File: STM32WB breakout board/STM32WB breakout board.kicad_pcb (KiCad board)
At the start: 2 copper layers, 70 x 80 mm, 37 parts, among them J1 Conn_02x10_Counter_Clockwise, J2 Conn_02x10_Counter_Clockwise, J3 RSP-122811-02, J4 Conn_02x10_Counter_Clockwise, J5 Conn_02x10_Counter_Clockwise, U1 STM32WB15CCU6, X1 32 MHz, X2 32.768 kHz

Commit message: PCB button updated
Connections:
- L2 pad 1: Net-(L2-Pad1) -> /RF & Power/VLXSMPS
- L2 pad 2: /RF & Power/VLXSMPS -> Net-(L2-Pad2)
- L3 pad 1: /RF & Power/VFBSMPS -> Net-(L2-Pad2)
- L3 pad 2: Net-(L2-Pad1) -> /RF & Power/VFBSMPS
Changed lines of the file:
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@@
   (net 36 "/RF & Power/VLXSMPS")
   (net 37 "unconnected-(U1-PB0-Pad28)")
-  (net 38 "Net-(L2-Pad1)")
+  (net 38 "Net-(L2-Pad2)")
   (net 39 "unconnected-(S1-NO_1-Pad1)")
   (net 40 "unconnected-(S1-COM_1-Pad3)")
@@
         (effects (font (size 1 1) (thickness 0.15)))
     )
-    (fp_text user "*" (at -4.491 -3.000756 unlocked) (layer "F.SilkS")
+    (fp_text user "*" (at -4.491 -3.000756) (layer "F.SilkS")
         (effects (font (size 1 1) (thickness 0.15)))
     )
-    (fp_text user "*" (at -4.491 -3.000756) (layer "F.SilkS")
+    (fp_text user "*" (at -4.491 -3.000756 unlocked) (layer "F.SilkS")
         (effects (font (size 1 1) (thickness 0.15)))
     )
@@
       (stroke (width 0.2) (type solid)) (fill none) (layer "F.Fab"))
     (pad "1" smd rect (at -0.468 0 180) (size 0.46 0.7) (layers "F.Cu" "F.Paste" "F.Mask")
-      (net 38 "Net-(L2-Pad1)") (pintype "passive") (solder_mask_margin 0.102))
-    (pad "2" smd rect (at 0.468 0 180) (size 0.46 0.7) (layers "F.Cu" "F.Paste" "F.Mask")
       (net 36 "/RF & Power/VLXSMPS") (pintype "passive") (solder_mask_margin 0.102))
+    (pad "2" smd rect (at 0.468 0 180) (size 0.46 0.7) (layers "F.Cu" "F.Paste" "F.Mask")
+      (net 38 "Net-(L2-Pad2)") (pintype "passive") (solder_mask_margin 0.102))
   )
   (footprint "Button_Switch_THT:TS026670BK160LCRD" (layer "F.Cu")
@@
     (property "ki_description" "Tactile Switches 6 x 6 mm, 7 mm Act Height, 160 gf, Black, Long Crimped, Through Hole, SPST,")
     (attr through_hole)
-    (fp_text reference "S1" (at 3.25 2.25) (layer "F.SilkS")
+    (fp_text reference "S1" (at 3.25 2.25 180) (layer "F.SilkS")
         (effects (font (size 1.27 1.27) (thickness 0.254)))
     )
-    (fp_text value "USER BUTTON" (at 3.25 2.25) (layer "F.SilkS") hide
+    (fp_text value "USER BUTTON" (at 3.25 2.25 180) (layer "F.SilkS") hide
         (effects (font (size 1.27 1.27) (thickness 0.254)))
     )
-    (fp_text user "${REFERENCE}" (at 3.25 2.25) (layer "F.Fab")
+    (fp_text user "${REFERENCE}" (at 3.25 2.25 180) (layer "F.Fab")
         (effects (font (size 1.27 1.27) (thickness 0.254)))
     )
@@
       (stroke (width 0.127) (type solid)) (layer "F.Fab"))
     (pad "1" smd rect (at -0.86 0 90) (size 1.2 1.47) (layers "F.Cu" "F.Paste" "F.Mask")
-      (net 35 "/RF & Power/VFBSMPS") (pintype "passive") (solder_mask_margin 0.102))
+      (net 38 "Net-(L2-Pad2)") (pintype "passive") (solder_mask_margin 0.102))
     (pad "2" smd rect (at 0.86 0 90) (size 1.2 1.47) (layers "F.Cu" "F.Paste" "F.Mask")
-      (net 38 "Net-(L2-Pad1)") (pintype "passive") (solder_mask_margin 0.102))
+      (net 35 "/RF & Power/VFBSMPS") (pintype "passive") (solder_mask_margin 0.102))
   )
   (footprint "GRM1555C1HR80BA01D:CAPC1005X55N" (layer "F.Cu")

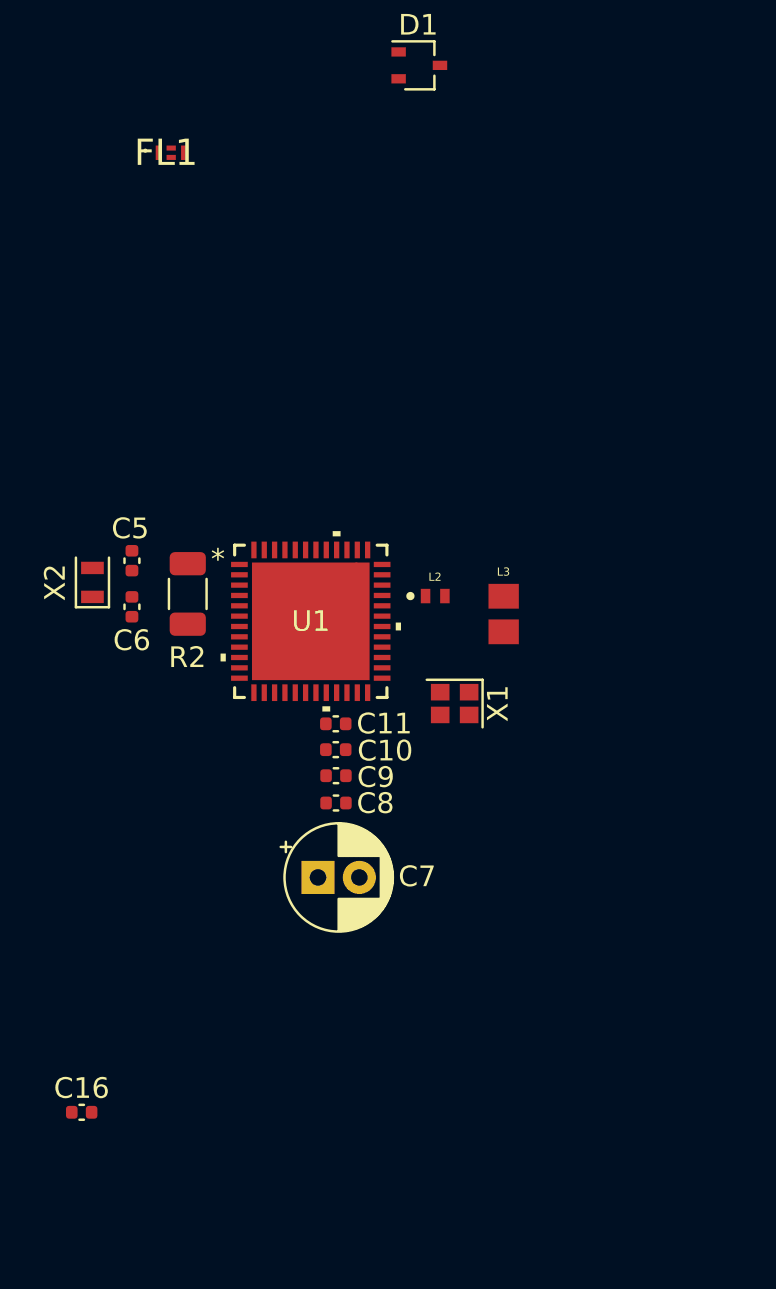
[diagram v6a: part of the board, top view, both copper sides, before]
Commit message: Regulator section updating
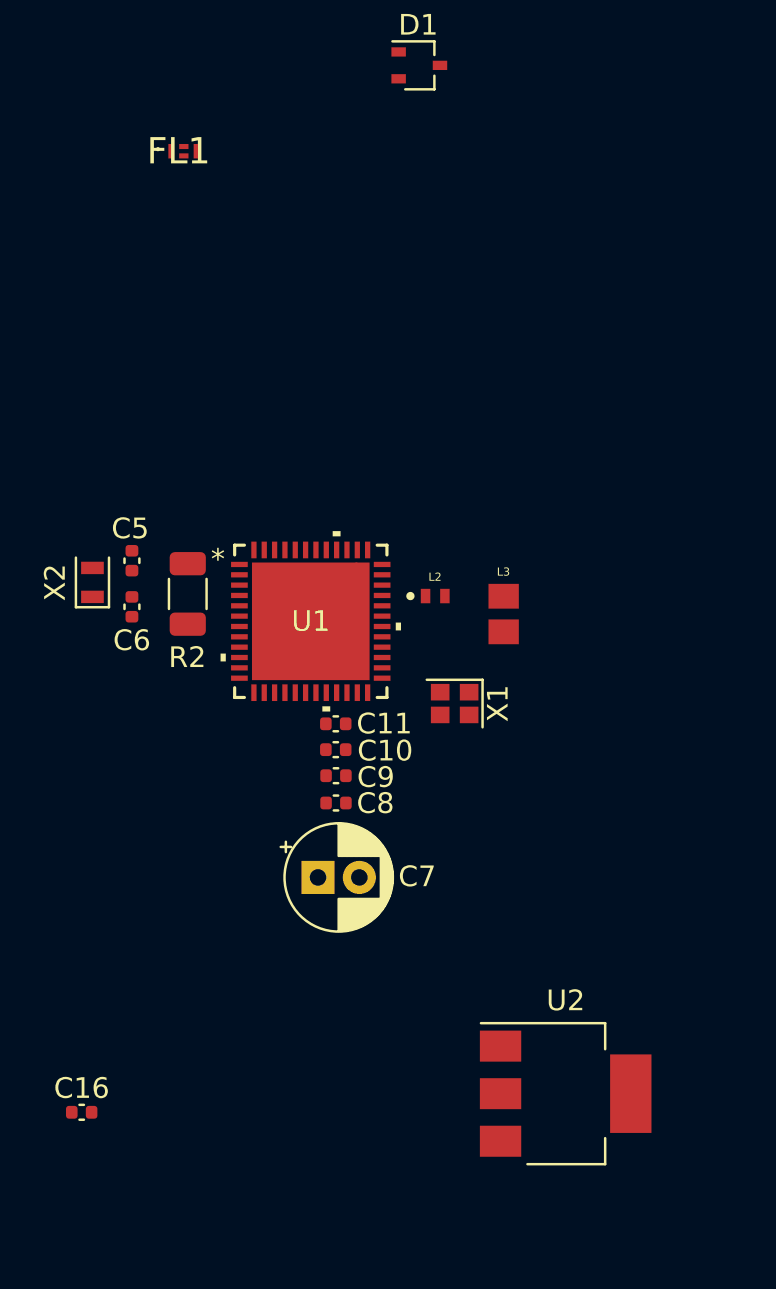
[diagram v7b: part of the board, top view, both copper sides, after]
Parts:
- added U2: AMS1117, Package_TO_SOT_SMD:SOT-223-3_TabPin2, F.Cu at (161.1, 117.7)
- moved FL1 0.61 mm to (142.6, 72.2)
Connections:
- net /RF & Power/RF1 renamed /RF & SMPS/RF1
- net /RF & Power/VFBSMPS renamed /RF & SMPS/VFBSMPS
- net /RF & Power/VLXSMPS renamed /RF & SMPS/VLXSMPS

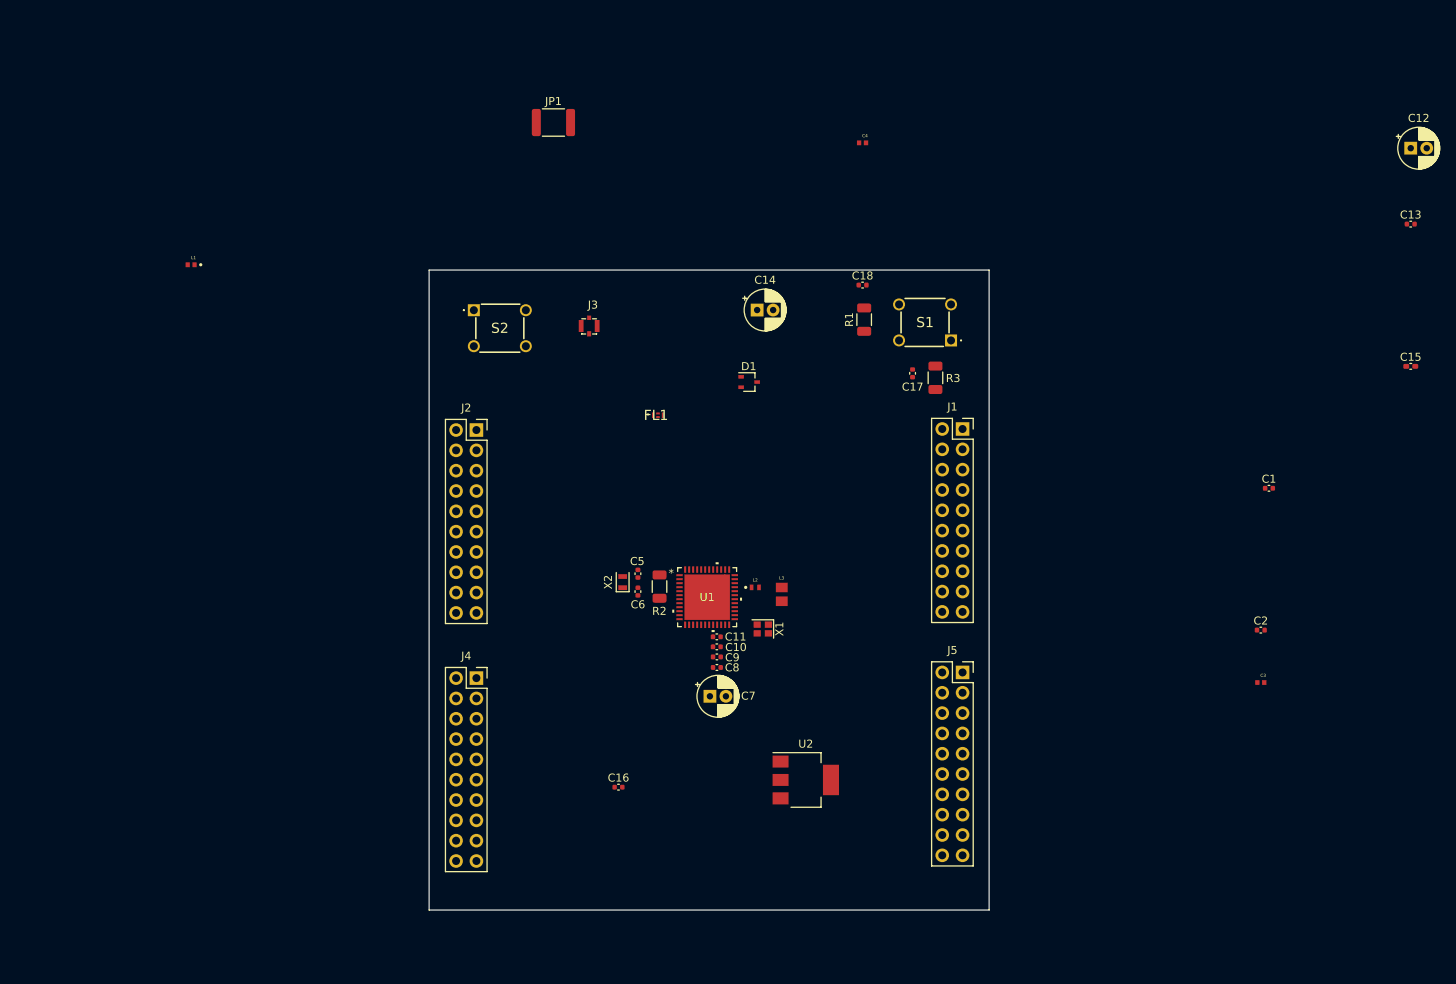
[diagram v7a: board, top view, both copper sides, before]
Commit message: Regulator section updating
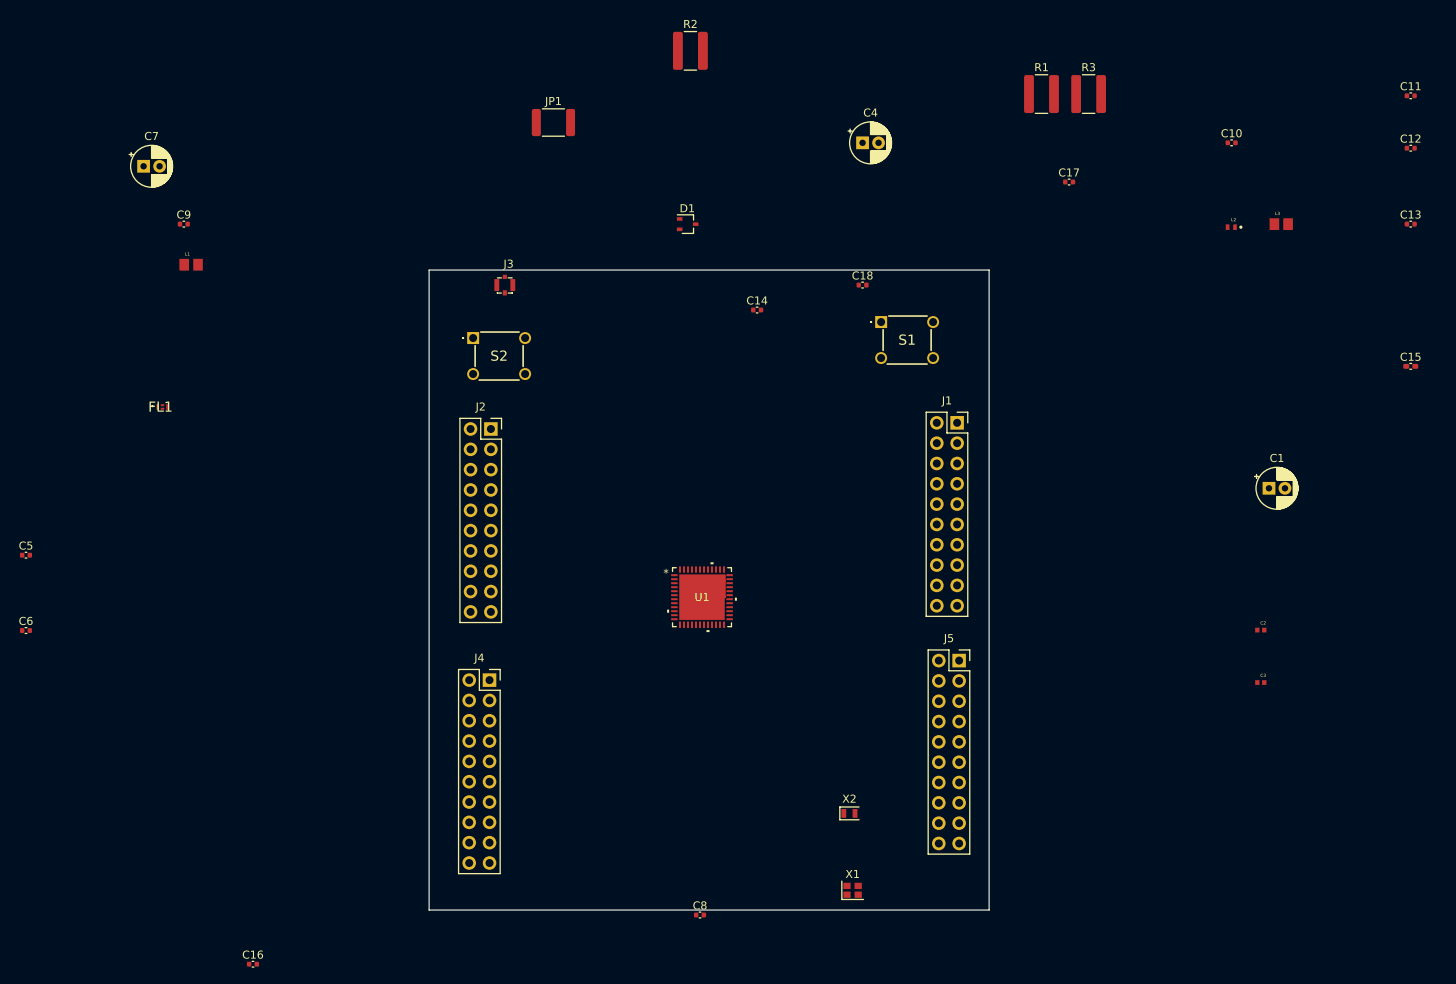
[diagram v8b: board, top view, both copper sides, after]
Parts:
- removed U2: AMS1117, Package_TO_SOT_SMD:SOT-223-3_TabPin2
- C1: value 100nF -> 4.7 uF; footprint Capacitor_SMD:C_0402_1005Metric -> Capacitor_THT:CP_Radial_D5.0mm_P2.00mm
- C12: value 4.7 uF -> 100nF; footprint Capacitor_THT:CP_Radial_D5.0mm_P2.00mm -> Capacitor_SMD:C_0402_1005Metric
- C14: value 4.7 uF -> 100 pF; footprint Capacitor_THT:CP_Radial_D5.0mm_P2.00mm -> Capacitor_SMD:C_0402_1005Metric
- C2: value 100 pF -> GRM1555C1HR80BA01D; footprint Capacitor_SMD:C_0402_1005Metric -> GRM1555C1HR80BA01D:CAPC1005X55N
- C3: value GRM1555C1HR80BA01D -> GRM1555C1HR30WA01D; footprint GRM1555C1HR80BA01D:CAPC1005X55N -> GRM1555C1HR30WA01D:CAPC1005X55N
- C4: value GRM1555C1HR30WA01D -> 4.7 uF; footprint GRM1555C1HR30WA01D:CAPC1005X55N -> Capacitor_THT:CP_Radial_D5.0mm_P2.00mm
- L1: value LQG15HS2N7S02D -> LQM21FN100M70L; footprint LQG15HS2N7S02D:INDC1005X55N -> LQM21FN100M70L:INDC2012X145N
- R1, R2, R3: footprint Resistor_SMD:R_1206_3216Metric -> Resistor_SMD:R_1218_3246Metric_Pad1.22x4.75mm_HandSolder
- moved C11 110.0 mm to (236.7, 32.2)
- moved C7 97.0 mm to (78.3, 41.0)
- moved C10 90.1 mm to (214.3, 38.1)
- moved C9 85.8 mm to (83.3, 48.3)
- moved L3 77.7 mm to (220.5, 48.3), turned to 0 degrees
- moved C6 76.6 mm to (63.6, 99.1), turned to 0 degrees
- moved C5 76.5 mm to (63.6, 89.6), turned to 0 degrees
- moved L2 74.6 mm to (214.3, 48.6), turned to 0 degrees
- moved R2 67.1 mm to (146.7, 26.6), turned to 0 degrees
- moved FL1 62.0 mm to (80.7, 71.1)
- moved C16 50.8 mm to (92.0, 140.8)
- moved X2 40.5 mm to (166.5, 121.9), turned to 0 degrees
- moved R3 40.3 mm to (196.4, 32.0), turned to 0 degrees
- moved R1 35.9 mm to (190.5, 32.0), turned to 0 degrees
- moved X1 34.5 mm to (166.9, 131.5), turned to 0 degrees
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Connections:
- net /MISO/PA6 renamed /PA6
- net /MOSI/PA5 renamed /PA5
- net /PA11 renamed /USB_N
- net /PA12 renamed /USB_P
- net /UART_RX/PA10 renamed /PA10
- net /UART_TX/PA9 renamed /PA9
- C1 pad 1: 3V3 -> /RF & Power/VFBSMPS
- C14 pad 1: /RF & SMPS/VFBSMPS -> 3V3
- C2 pad 1: 3V3 -> GND
- C2 pad 2: GND -> /RF & Power/RF1
- C3 pad 2: /RF & SMPS/RF1 -> Net-(FL1-IN)
- C4 pad 1: GND -> 3V3
- C4 pad 2: Net-(FL1-IN) -> GND
- J1 pad 13: /PE4 -> unconnected-(J1-Pin_13-Pad13)
- J1 pad 16: /SCK/PA1 -> /PA1
- J2 pad 9: unconnected-(J2-Pin_9-Pad9) -> /PE4
- J4 pad 13: /PE4 -> unconnected-(J4-Pin_13-Pad13)
- J4 pad 16: /SCK/PA1 -> /PA1
- J5 pad 9: unconnected-(J5-Pin_9-Pad9) -> /PE4
- L1 pad 1: /RF & SMPS/RF1 -> /RF & Power/VFBSMPS
- L1 pad 2: Net-(FL1-IN) -> Net-(L1-Pad2)
- L2 pad 1: /RF & SMPS/VLXSMPS -> Net-(L1-Pad2)
- L2 pad 2: Net-(L2-Pad2) -> /RF & Power/VLXSMPS
- L3 pad 1: Net-(L2-Pad2) -> /RF & Power/VFBSMPS
- L3 pad 2: /RF & SMPS/VFBSMPS -> Net-(L2-Pad1)
- U1 pad 10: /SCK/PA1 -> unconnected-(U1-PA1-Pad10)
- U1 pad 22: GND -> /VSSRF
- U1 pad 32: GND -> /VSSSMPS
- U1 pad 40: 3V3 -> /VDDUSB
